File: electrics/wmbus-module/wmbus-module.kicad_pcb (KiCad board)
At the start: 2 copper layers, 86 x 31 mm, 25 parts, among them J1 North, J2 South, J3 West, J4 East, U1 BA033CC0FP-E2, U2 MAX3486, U3 MAX3486

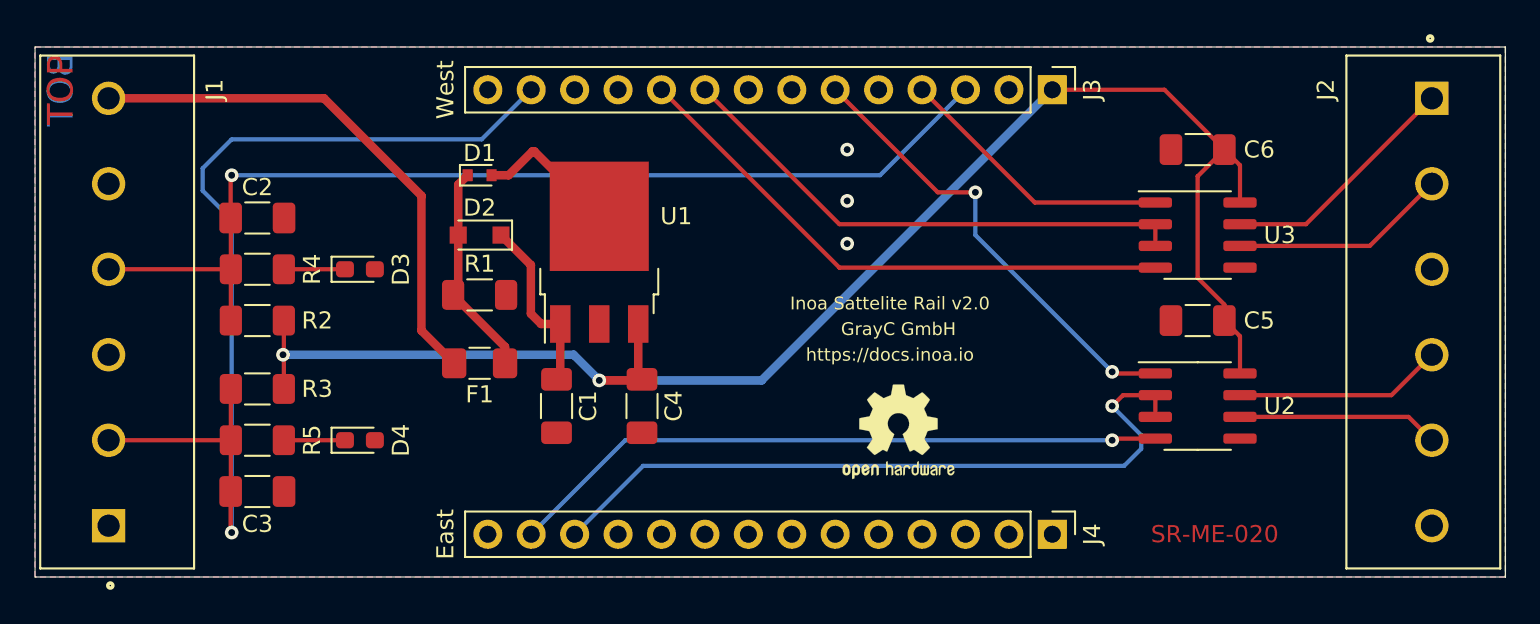
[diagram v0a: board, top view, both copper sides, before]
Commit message: Fix all ERC and DRC warnings during build
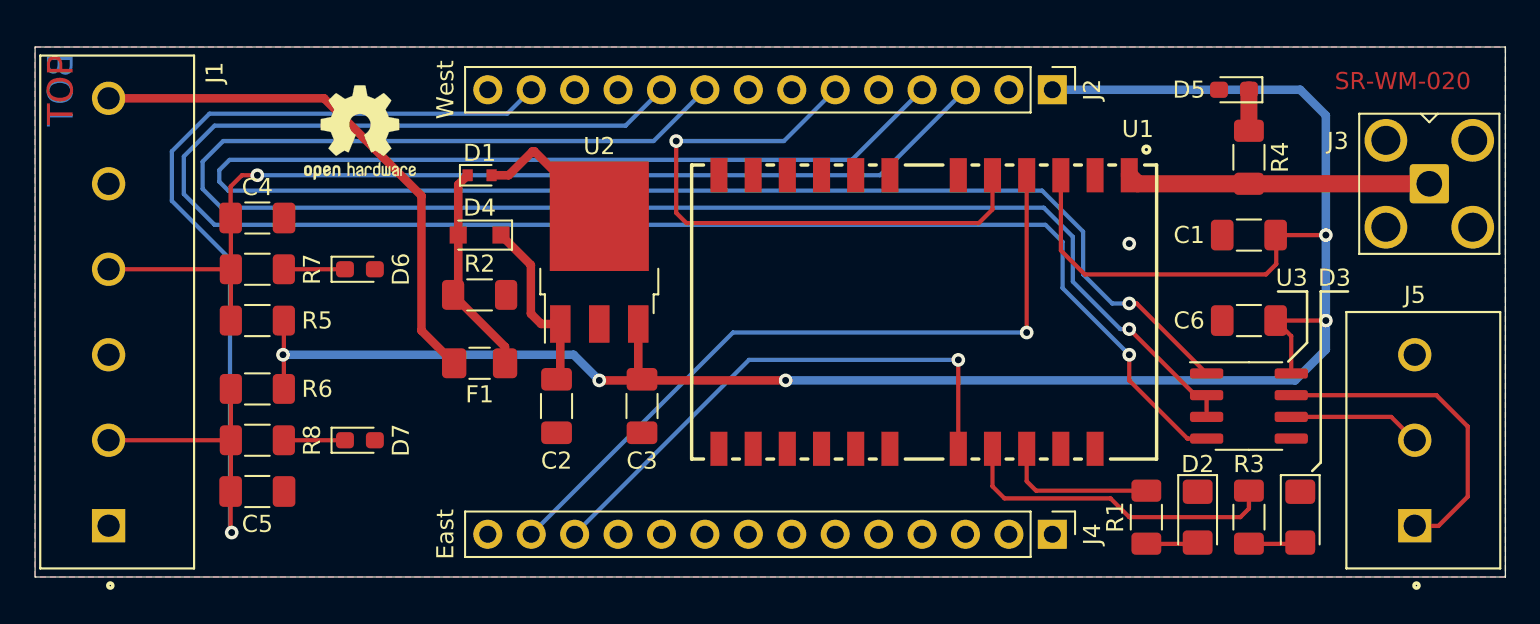
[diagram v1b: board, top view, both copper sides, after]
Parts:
- removed the C5 at (174.0, 107.0)
- removed the U2 at (174.0, 112.0)
- added C1: 100uF, Capacitor_SMD:C_1206_3216Metric_Pad1.33x1.80mm_HandSolder, F.Cu at (177.0, 102.0)
- added D2: TX, LED_SMD:LED_1206_3216Metric_Pad1.42x1.75mm_HandSolder, F.Cu at (174.0, 118.5)
- added D3: RX, LED_SMD:LED_1206_3216Metric_Pad1.42x1.75mm_HandSolder, F.Cu at (180.0, 118.5)
- added D5: D_TVS, Diode_SMD:D_0603_1608Metric_Pad1.05x0.95mm_HandSolder, F.Cu at (176.1, 93.5)
- added J4: East, Connector_PinHeader_2.54mm:PinHeader_1x14_P2.54mm_Vertical, F.Cu at (165.5, 119.5)
- added R1: 220R, Resistor_SMD:R_1206_3216Metric_Pad1.30x1.75mm_HandSolder, F.Cu at (171.0, 118.5)
- added R3: 220R, Resistor_SMD:R_1206_3216Metric_Pad1.30x1.75mm_HandSolder, F.Cu at (177.0, 118.5)
- added R4: 220R, Resistor_SMD:R_1206_3216Metric_Pad1.30x1.75mm_HandSolder, F.Cu at (177.0, 97.5)
- added U1: Metis-I, footprints:WE-FP-1, F.Cu at (158.0, 106.5)
- J2: value South -> West; footprint footprints:PHOENIX_1935200 -> Connector_PinHeader_2.54mm:PinHeader_1x14_P2.54mm_Vertical
- J3: value West -> WMBus; footprint Connector_PinHeader_2.54mm:PinHeader_1x14_P2.54mm_Vertical -> Connector_Coaxial:SMA_Amphenol_901-143_Horizontal
- J5: renamed from J4; value East -> South; footprint Connector_PinHeader_2.54mm:PinHeader_1x14_P2.54mm_Vertical -> footprints:PHOENIX_1711039
- moved G1 36.0 mm to (125.0, 96.0)
- moved J2 25.7 mm to (165.5, 93.5)
- moved J3 22.7 mm to (187.6, 99.0)
- moved J5 21.9 mm to (186.7, 114.0), turned to 90 degrees
- moved C6 10.4 mm to (177.0, 107.0)
- moved U3 10.4 mm to (177.0, 112.0)
- renumbered C1 to C2, C4 to C3, C2 to C4, C3 to C5, D2 to D4, D3 to D6, D4 to D7, R1 to R2, R2 to R5, R3 to R6, R4 to R7, R5 to R8, U1 to U2
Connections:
- J2 pad 1: RS485_0_B -> +3V3
- J2 pad 2: RS485_0_A -> unconnected-(J2-Pad2)
- J2 pad 3: GND -> S0_0
- J2 pad 4: RS485_1_B -> RS485_0_RX
- J2 pad 5: RS485_1_A -> unconnected-(J2-Pad5)
- J2 pad 6: GND -> WMBus_RX
- J3 pad 1: +3V3 -> Antenna
- J3 pad 2: unconnected-(J3-Pad2) -> GND
- J5 pad 1: GND -> RS485_0_B
- J5 pad 2: unconnected-(J4-Pad2) -> RS485_0_A
- J5 pad 3: unconnected-(J4-Pad3) -> GND
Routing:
- net RS485_0_RX: track 16.4 -> 107.6 mm, vias 0 -> 1
- net RS485_0_TXE: track 30.9 -> 99.2 mm, vias 0 -> 1
- net RS485_0_TX: track 33.2 -> 100.0 mm, vias 0 -> 1
- net WMBus_TX: track 0.00 -> 43.1 mm, vias 0 -> 1
- net RS485_1_TXE: track 42.5 -> 0.00 mm, vias 1 -> 0
- net RS485_1_TX: track 38.8 -> 0.00 mm, vias 1 -> 0
- net +3V3: track 92.4 -> 129.1 mm, vias 2 -> 5
- net WMBus_RX: track 0.00 -> 35.8 mm, vias 0 -> 1
- net ~{WMBus_Reset}: track 0.00 -> 31.9 mm, vias 0 -> 1
- net RS485_1_RX: track 27.1 -> 0.00 mm, vias 2 -> 0
- net RX_IND: track 0.00 -> 19.2 mm
- net Antenna: track 0.00 -> 17.7 mm
- net RS485_1_B: track 12.2 -> 0.00 mm
- net RS485_1_A: track 11.8 -> 0.00 mm
- net TX_IND: track 0.00 -> 9.13 mm
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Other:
- board text added: "SR-WM-020"
- board text removed: "SR-ME-020"
